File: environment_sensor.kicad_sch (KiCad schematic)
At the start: 123 parts, among them J17 USB-C_GCT_USB4145-03-0070-C, J18 JST_SH_1x4_SM04B-SRSS-TB-LF-SN, J20 JST_SH_1x4_SM04B-SRSS-TB-LF-SN, U11 FT4232H_VQFN, U27 AP7370-33SA-7, U28 STM32G474CET6, U29 MB85RC1MTPNF-G, U30 SHT45, U31 BME280, Y2 ABM3B-12.000MHZ-B2-T, Y3 ECS-_327-12_5-34B-TR, Y4 ABM3B-8.000MHZ-10-1-U-T

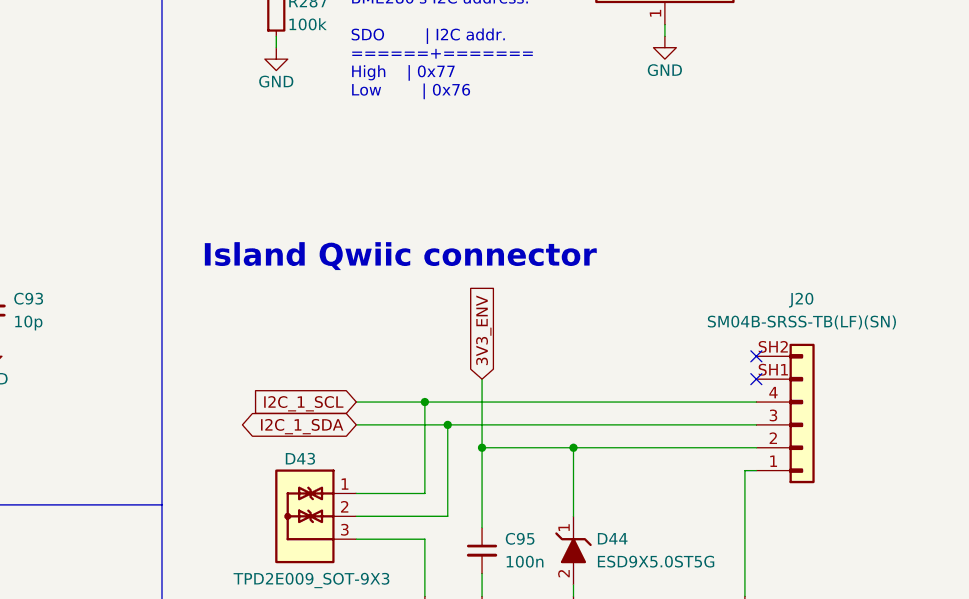
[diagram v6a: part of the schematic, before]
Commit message: Add env sensor onto the board
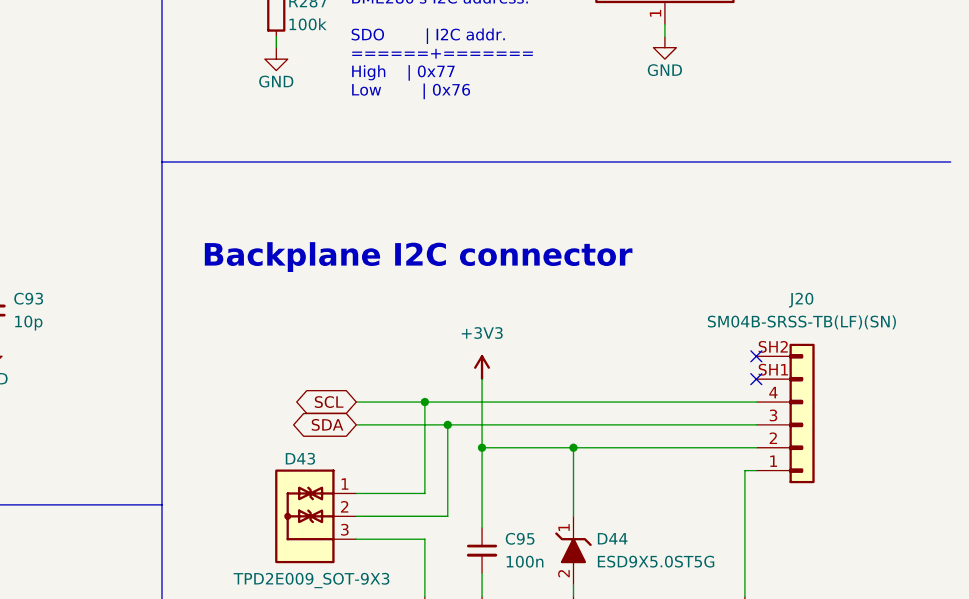
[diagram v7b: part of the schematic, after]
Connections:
- net +3V3: now also C95.1, D44.1, J20.2
- net 3V3_ENV: no longer C95.1, D44.1, J20.2
- net I2C_1_SCL: no longer D43.1, J20.4
- net I2C_1_SDA: no longer D43.2, J20.3
- new net SCL: D43.1, J20.4
- new net SDA: D43.2, J20.3
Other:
- note added: "Backplane I2C connector"
- note removed: "Island Qwiic connector"
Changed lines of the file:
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@@
     (stroke (width 0) (type default) (color 0 0 0 0))
   )
+  (polyline (pts (xy 320.04 194.31) (xy 407.67 194.31))
+    (stroke (width 0) (type default) (color 0 0 0 0))
+  )
   (wire (pts (xy 135.89 49.53) (xy 135.89 48.26))
     (stroke (width 0) (type default) (color 0 0 0 0))
@@
     (effects (font (size 2.5 2.5) (thickness 0.6) bold) (justify left bottom))
   )
-  (text "Island Qwiic connector" (at 324.485 206.375 0)
+  (text "Backplane I2C connector" (at 324.485 206.375 0)
     (effects (font (size 2.5 2.5) (thickness 0.5) bold) (justify left bottom))
   )
@@
     )
   )
-  (global_label "I2C_1_SCL" (shape input) (at 341.63 220.98 180) (fields_autoplaced)
+  (global_label "I2C_1_SCL" (shape input) (at 351.79 130.81 180) (fields_autoplaced)
     (effects (font (size 1.27 1.27)) (justify right))
-    (property "Intersheet References" "${INTERSHEET_REFS}" (id 0) (at 329.4802 220.9006 0)
+    (property "Intersheet References" "${INTERSHEET_REFS}" (id 0) (at 339.6402 130.7306 0)
       (effects (font (size 1.27 1.27)) (justify right) hide)
     )
   )
-  (global_label "I2C_1_SCL" (shape input) (at 351.79 130.81 180) (fields_autoplaced)
+  (global_label "SCL" (shape bidirectional) (at 341.63 220.98 180) (fields_autoplaced)
     (effects (font (size 1.27 1.27)) (justify right))
-    (property "Intersheet References" "${INTERSHEET_REFS}" (id 0) (at 339.6402 130.7306 0)
-      (effects (font (size 1.27 1.27)) (justify right) hide)
+    (property "Intersheet References" "${INTERSHEET_REFS}" (id 0) (at 445.77 456.565 0)
+      (effects (font (size 1.27 1.27)) hide)
     )
   )
@@
     )
   )
-  (global_label "JTDI" (shape bidirectional) (at 215.9 179.07 180) (fields_autoplaced)
+  (global_label "SDA" (shape bidirectional) (at 341.63 223.52 180) (fields_autoplaced)
     (effects (font (size 1.27 1.27)) (justify right))
-    (property "Intersheet References" "${INTERSHEET_REFS}" (id 0) (at 209.6769 178.9906 0)
-      (effects (font (size 1.27 1.27)) (justify right) hide)
+    (property "Intersheet References" "${INTERSHEET_REFS}" (id 0) (at 445.77 456.565 0)
+      (effects (font (size 1.27 1.27)) hide)
     )
   )
-  (global_label "I2C_1_SDA" (shape bidirectional) (at 341.63 223.52 180) (fields_autoplaced)
+  (global_label "JTDI" (shape bidirectional) (at 215.9 179.07 180) (fields_autoplaced)
     (effects (font (size 1.27 1.27)) (justify right))
-    (property "Intersheet References" "${INTERSHEET_REFS}" (id 0) (at 329.4198 223.4406 0)
+    (property "Intersheet References" "${INTERSHEET_REFS}" (id 0) (at 209.6769 178.9906 0)
       (effects (font (size 1.27 1.27)) (justify right) hide)
     )
@@
     )
   )
-  (global_label "3V3_ENV" (shape input) (at 355.6 218.44 90) (fields_autoplaced)
-    (effects (font (size 1.27 1.27)) (justify left))
-    (property "Intersheet References" "${INTERSHEET_REFS}" (id 0) (at 355.5206 208.0725 90)
-      (effects (font (size 1.27 1.27)) (justify left) hide)
-    )
-  )
   (global_label "LPUART_1_STM_TX" (shape input) (at 163.83 205.74 0) (fields_autoplaced)
     (effects (font (size 1.27 1.27)) (justify left))
@@
     (pin "2")
   )
+  (symbol (lib_id "environment-sensor:+3V3") (at 355.6 218.44 0) (unit 1)
+    (in_bom yes) (on_board yes) (fields_autoplaced)
+    (property "Reference" "#PWR?" (id 0) (at 355.6 222.25 0)
+      (effects (font (size 1.27 1.27)) hide)
+    )
+    (property "Value" "+3V3" (id 1) (at 355.6 213.36 0))
+    (property "Footprint" "" (id 2) (at 355.6 218.44 0)
+      (effects (font (size 1.27 1.27)) hide)
+    )
+    (property "Datasheet" "" (id 3) (at 355.6 218.44 0)
+      (effects (font (size 1.27 1.27)) hide)
+    )
+    (property "Author" "Antmicro" (id 4) (at 370.84 226.06 0)
+      (effects (font (size 1.27 1.27) (thickness 0.15)) (justify left bottom) hide)
+    )
+    (property "License" "Apache-2.0" (id 5) (at 370.84 228.6 0)
+      (effects (font (size 1.27 1.27) (thickness 0.15)) (justify left bottom) hide)
+    )
+    (pin "1")
+  )
   (symbol (lib_id "environment-sensor:GND") (at 214.63 55.88 0) (unit 1)

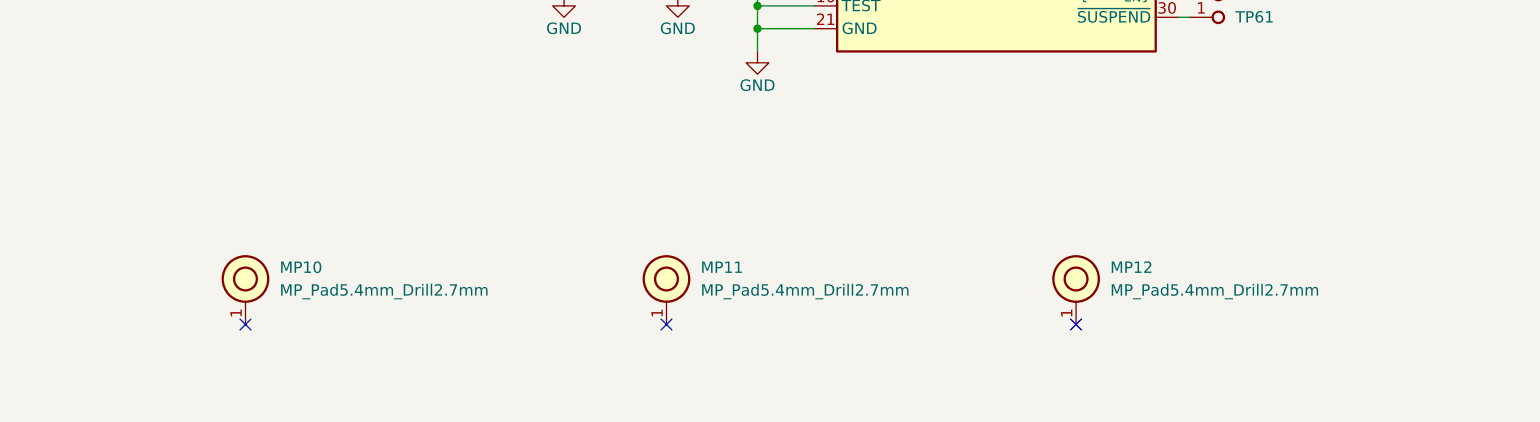
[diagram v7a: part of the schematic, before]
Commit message: Replace old studs with new 10mm M2 model
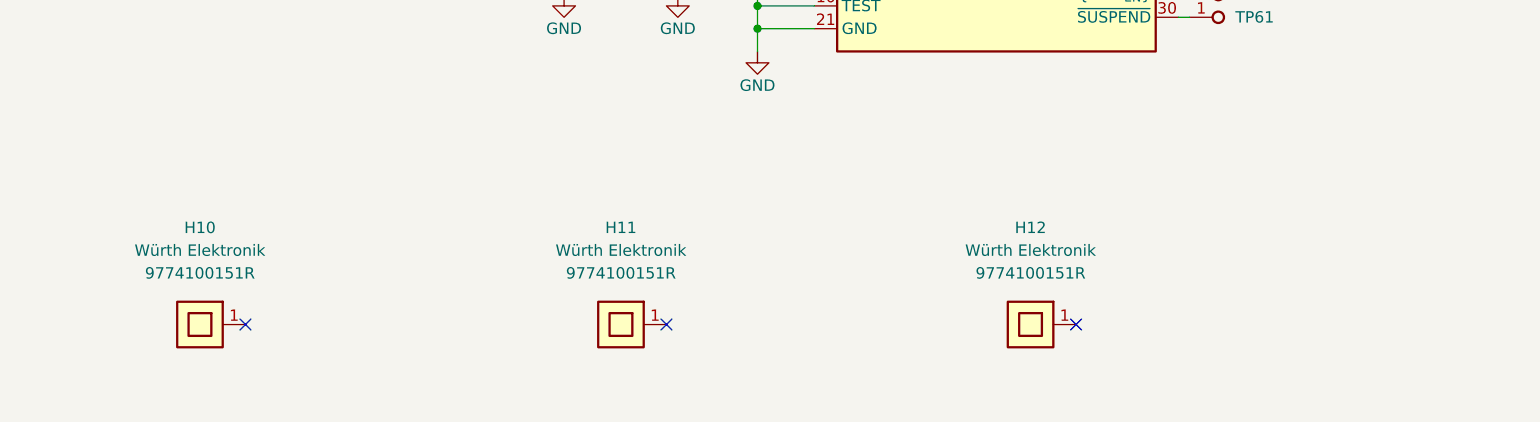
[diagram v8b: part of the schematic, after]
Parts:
- removed MP10, MP11, MP12: MP_Pad5.4mm_Drill2.7mm, antmicro-footprints:MP_Pad5.4mm_Drill2.7mm, symbol antmicroMechanicalParts:MP_Pad5.4mm_Drill2.7mm
- added H10, H11, H12: Spacer_Drill3.7mm_H10mm_9774100151R, antmicro-footprints:Spacer_Drill3.7mm_H10mm_9774100151R, symbol antmicroMechanicalParts:Spacer_Drill3.7mm_H10mm_9774100151R
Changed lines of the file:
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@@
     (pin "2")
   )
+  (symbol (lib_id "antmicroMechanicalParts:Spacer_Drill3.7mm_H10mm_9774100151R") (at 38.1 276.86 180) (unit 1)
+    (in_bom yes) (on_board yes) (fields_autoplaced)
+    (property "Reference" "H10" (id 0) (at 33.02 266.065 0)
+      (effects (font (size 1.27 1.27) (thickness 0.15)))
+    )
+    (property "Value" "Spacer_Drill3.7mm_H10mm_9774100151R" (id 1) (at 22.86 264.16 0)
+      (effects (font (size 1.27 1.27) (thickness 0.15)) (justify left bottom) hide)
+    )
+    (property "Footprint" "antmicro-footprints:Spacer_Drill3.7mm_H10mm_9774100151R" (id 2) (at 22.86 261.62 0)
+      (effects (font (size 1.27 1.27) (thickness 0.15)) (justify left bottom) hide)
+    )
+    (property "Datasheet" "https://www.we-online.com/components/products/datasheet/9774100151R.pdf" (id 3) (at 22.86 259.08 0)
+      (effects (font (size 1.27 1.27) (thickness 0.15)) (justify left bottom) hide)
+    )
+    (property "Manufacturer" "Würth Elektronik" (id 4) (at 33.02 268.605 0)
+      (effects (font (size 1.27 1.27) (thickness 0.15)))
+    )
+    (property "MPN" "9774100151R" (id 5) (at 33.02 271.145 0)
+      (effects (font (size 1.27 1.27) (thickness 0.15)))
+    )
+    (property "Author" "Antmicro" (id 6) (at 22.86 256.54 0)
+      (effects (font (size 1.27 1.27) (thickness 0.15)) (justify left bottom) hide)
+    )
+    (property "License" "Apache-2.0" (id 7) (at 22.86 254 0)
+      (effects (font (size 1.27 1.27) (thickness 0.15)) (justify left bottom) hide)
+    )
+    (pin "1")
+  )
   (symbol (lib_id "antmicroTestPoints:TP_1mm_SMD") (at 391.16 52.07 0) (unit 1)
     (in_bom yes) (on_board yes) (fields_autoplaced)
@@
     (pin "2")
   )
-  (symbol (lib_id "antmicroMechanicalParts:MP_Pad5.4mm_Drill2.7mm") (at 130.81 276.86 90) (unit 1)
-    (in_bom yes) (on_board yes) (fields_autoplaced)
-    (property "Reference" "MP12" (id 0) (at 134.62 270.5099 90)
-      (effects (font (size 1.27 1.27) (thickness 0.15)) (justify right))
-    )
-    (property "Value" "MP_Pad5.4mm_Drill2.7mm" (id 1) (at 134.62 273.0499 90)
-      (effects (font (size 1.27 1.27) (thickness 0.15)) (justify right))
-    )
-    (property "Footprint" "antmicro-footprints:MP_Pad5.4mm_Drill2.7mm" (id 2) (at 138.43 256.54 0)
-      (effects (font (size 1.27 1.27) (thickness 0.15)) (justify left bottom) hide)
-    )
-    (property "Datasheet" "" (id 3) (at 146.38 260.02 0)
-      (effects (font (size 1.27 1.27) (thickness 0.15)) (justify left bottom) hide)
-    )
-    (property "Author" "Antmicro" (id 4) (at 140.97 256.54 0)
-      (effects (font (size 1.27 1.27) (thickness 0.15)) (justify left bottom) hide)
-    )
-    (property "License" "Apache-2.0" (id 5) (at 143.51 256.54 0)
-      (effects (font (size 1.27 1.27) (thickness 0.15)) (justify left bottom) hide)
-    )
-    (pin "1")
-  )
   (symbol (lib_id "environment-sensor:FT4232H_VQFN") (at 101.6 152.4 0) (unit 1)
     (in_bom yes) (on_board yes) (fields_autoplaced)
@@
     (pin "1")
   )
+  (symbol (lib_id "antmicroMechanicalParts:Spacer_Drill3.7mm_H10mm_9774100151R") (at 85.09 276.86 180) (unit 1)
+    (in_bom yes) (on_board yes) (fields_autoplaced)
+    (property "Reference" "H11" (id 0) (at 80.01 266.065 0)
+      (effects (font (size 1.27 1.27) (thickness 0.15)))
+    )
+    (property "Value" "Spacer_Drill3.7mm_H10mm_9774100151R" (id 1) (at 69.85 264.16 0)
+      (effects (font (size 1.27 1.27) (thickness 0.15)) (justify left bottom) hide)
+    )
+    (property "Footprint" "antmicro-footprints:Spacer_Drill3.7mm_H10mm_9774100151R" (id 2) (at 69.85 261.62 0)
+      (effects (font (size 1.27 1.27) (thickness 0.15)) (justify left bottom) hide)
+    )
+    (property "Datasheet" "https://www.we-online.com/components/products/datasheet/9774100151R.pdf" (id 3) (at 69.85 259.08 0)
+      (effects (font (size 1.27 1.27) (thickness 0.15)) (justify left bottom) hide)
+    )
+    (property "Manufacturer" "Würth Elektronik" (id 4) (at 80.01 268.605 0)
+      (effects (font (size 1.27 1.27) (thickness 0.15)))
+    )
+    (property "MPN" "9774100151R" (id 5) (at 80.01 271.145 0)
+      (effects (font (size 1.27 1.27) (thickness 0.15)))
+    )
+    (property "Author" "Antmicro" (id 6) (at 69.85 256.54 0)
+      (effects (font (size 1.27 1.27) (thickness 0.15)) (justify left bottom) hide)
+    )
+    (property "License" "Apache-2.0" (id 7) (at 69.85 254 0)
+      (effects (font (size 1.27 1.27) (thickness 0.15)) (justify left bottom) hide)
+    )
+    (pin "1")
+  )
   (symbol (lib_id "environment-sensor:GND") (at 355.6 242.57 0) (mirror y) (unit 1)
     (in_bom yes) (on_board yes)
@@
     (pin "2")
   )
-  (symbol (lib_id "antmicroMechanicalParts:MP_Pad5.4mm_Drill2.7mm") (at 85.09 276.86 90) (unit 1)
-    (in_bom yes) (on_board yes) (fields_autoplaced)
-    (property "Reference" "MP11" (id 0) (at 88.9 270.5099 90)
-      (effects (font (size 1.27 1.27) (thickness 0.15)) (justify right))
-    )
-    (property "Value" "MP_Pad5.4mm_Drill2.7mm" (id 1) (at 88.9 273.0499 90)
-      (effects (font (size 1.27 1.27) (thickness 0.15)) (justify right))
-    )
-    (property "Footprint" "antmicro-footprints:MP_Pad5.4mm_Drill2.7mm" (id 2) (at 92.71 256.54 0)
-      (effects (font (size 1.27 1.27) (thickness 0.15)) (justify left bottom) hide)
-    )
-    (property "Datasheet" "" (id 3) (at 100.66 260.02 0)
-      (effects (font (size 1.27 1.27) (thickness 0.15)) (justify left bottom) hide)
-    )
-    (property "Author" "Antmicro" (id 4) (at 95.25 256.54 0)
-      (effects (font (size 1.27 1.27) (thickness 0.15)) (justify left bottom) hide)
-    )
-    (property "License" "Apache-2.0" (id 5) (at 97.79 256.54 0)
-      (effects (font (size 1.27 1.27) (thickness 0.15)) (justify left bottom) hide)
-    )
-    (pin "1")
-  )
   (symbol (lib_id "environment-sensor:C_4u7_0402") (at 191.77 118.11 90) (unit 1)
     (in_bom yes) (on_board yes) (fields_autoplaced)
@@
   (symbol (lib_id "environment-sensor:+3V3") (at 355.6 218.44 0) (unit 1)
     (in_bom yes) (on_board yes) (fields_autoplaced)
-    (property "Reference" "#PWR?" (id 0) (at 355.6 222.25 0)
+    (property "Reference" "#PWR0208" (id 0) (at 355.6 222.25 0)
       (effects (font (size 1.27 1.27)) hide)
     )
@@
     (pin "2")
   )
+  (symbol (lib_id "antmicroMechanicalParts:Spacer_Drill3.7mm_H10mm_9774100151R") (at 130.81 276.86 180) (unit 1)
+    (in_bom yes) (on_board yes) (fields_autoplaced)
+    (property "Reference" "H12" (id 0) (at 125.73 266.065 0)
+      (effects (font (size 1.27 1.27) (thickness 0.15)))
+    )
+    (property "Value" "Spacer_Drill3.7mm_H10mm_9774100151R" (id 1) (at 115.57 264.16 0)
+      (effects (font (size 1.27 1.27) (thickness 0.15)) (justify left bottom) hide)
+    )
+    (property "Footprint" "antmicro-footprints:Spacer_Drill3.7mm_H10mm_9774100151R" (id 2) (at 115.57 261.62 0)
+      (effects (font (size 1.27 1.27) (thickness 0.15)) (justify left bottom) hide)
+    )
+    (property "Datasheet" "https://www.we-online.com/components/products/datasheet/9774100151R.pdf" (id 3) (at 115.57 259.08 0)
+      (effects (font (size 1.27 1.27) (thickness 0.15)) (justify left bottom) hide)
+    )
+    (property "Manufacturer" "Würth Elektronik" (id 4) (at 125.73 268.605 0)
+      (effects (font (size 1.27 1.27) (thickness 0.15)))
+    )
+    (property "MPN" "9774100151R" (id 5) (at 125.73 271.145 0)
+      (effects (font (size 1.27 1.27) (thickness 0.15)))
+    )
+    (property "Author" "Antmicro" (id 6) (at 115.57 256.54 0)
+      (effects (font (size 1.27 1.27) (thickness 0.15)) (justify left bottom) hide)
+    )
+    (property "License" "Apache-2.0" (id 7) (at 115.57 254 0)
+      (effects (font (size 1.27 1.27) (thickness 0.15)) (justify left bottom) hide)
+    )
+    (pin "1")
+  )
   (symbol (lib_id "environment-sensor:FB_120Z_2A_0603") (at 248.92 102.87 0) (mirror y) (unit 1)
     (in_bom yes) (on_board yes) (fields_autoplaced)
@@
     (pin "2")
   )
-  (symbol (lib_id "antmicroMechanicalParts:MP_Pad5.4mm_Drill2.7mm") (at 38.1 276.86 90) (unit 1)
-    (in_bom yes) (on_board yes) (fields_autoplaced)
-    (property "Reference" "MP10" (id 0) (at 41.91 270.5099 90)
-      (effects (font (size 1.27 1.27) (thickness 0.15)) (justify right))
-    )
-    (property "Value" "MP_Pad5.4mm_Drill2.7mm" (id 1) (at 41.91 273.0499 90)
-      (effects (font (size 1.27 1.27) (thickness 0.15)) (justify right))
-    )
-    (property "Footprint" "antmicro-footprints:MP_Pad5.4mm_Drill2.7mm" (id 2) (at 45.72 256.54 0)
-      (effects (font (size 1.27 1.27) (thickness 0.15)) (justify left bottom) hide)
-    )
-    (property "Datasheet" "" (id 3) (at 53.67 260.02 0)
-      (effects (font (size 1.27 1.27) (thickness 0.15)) (justify left bottom) hide)
-    )
-    (property "Author" "Antmicro" (id 4) (at 48.26 256.54 0)
-      (effects (font (size 1.27 1.27) (thickness 0.15)) (justify left bottom) hide)
-    )
-    (property "License" "Apache-2.0" (id 5) (at 50.8 256.54 0)
-      (effects (font (size 1.27 1.27) (thickness 0.15)) (justify left bottom) hide)
-    )
-    (pin "1")
-  )
   (symbol (lib_id "environment-sensor:GND") (at 95.25 246.38 0) (unit 1)
